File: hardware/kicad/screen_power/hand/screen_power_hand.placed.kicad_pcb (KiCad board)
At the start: 4 copper layers, 130 x 120 mm, 56 parts, among them J1 AUX 5V INPUT, J101 PI USB, J102 TOUCH, J103 EVM 5V, J104 EVM CONTROL, J2 SCREEN CONTROL, J201 PI USB, J202 TOUCH, J203 EVM 5V, J204 EVM CONTROL, K101 G6K-2P-RF DC5, K102 G5LE-1 DC5, K201 G6K-2P-RF DC5, K202 G5LE-1 DC5, Q1 2N3904, Q101 2N7000, Q102 2N3906, Q103 IRLZ44NPBF, Q104 2N7000, Q201 2N7000, Q202 2N3906, Q203 IRLZ44NPBF, Q204 2N7000

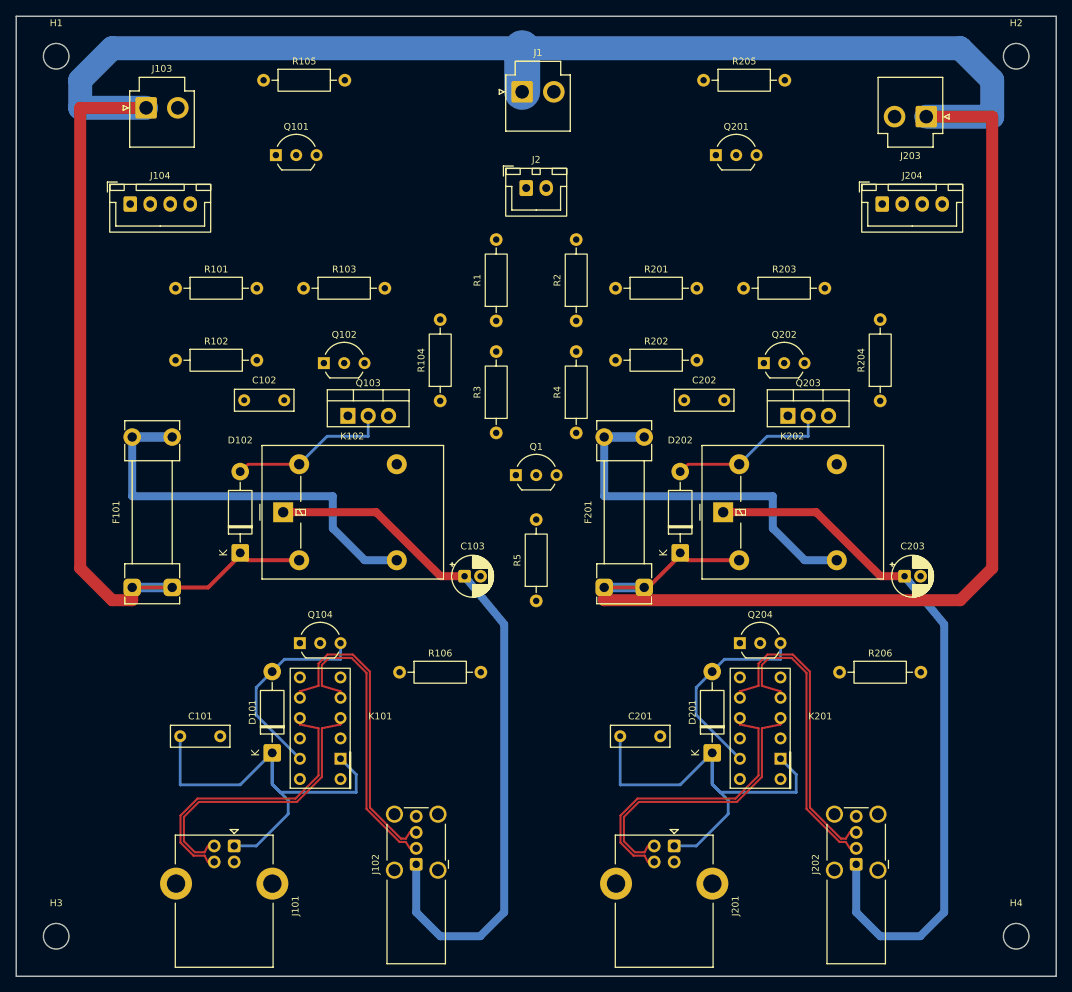
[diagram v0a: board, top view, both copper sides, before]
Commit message: refactor(hardware): simplify and compact screen power boards
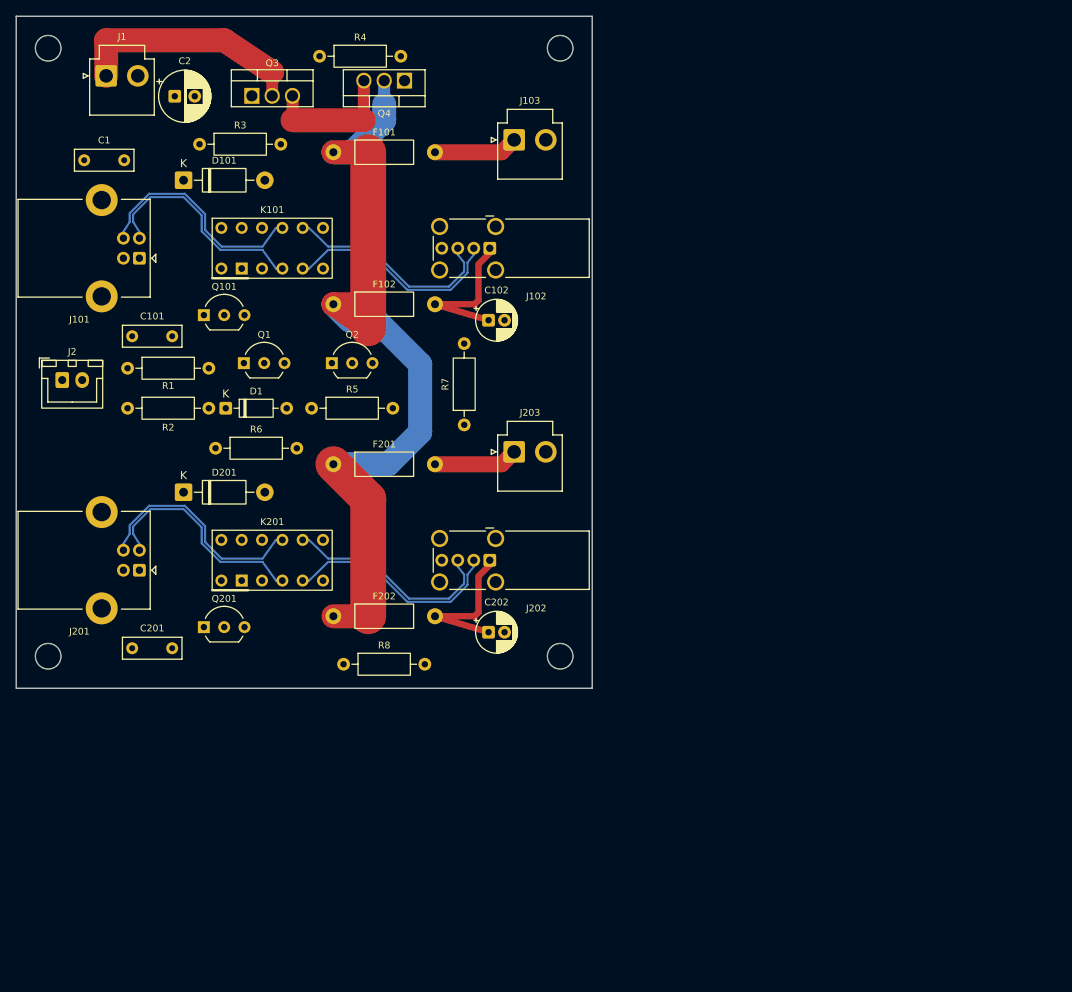
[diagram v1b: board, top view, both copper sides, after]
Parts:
- removed C103, C203: 150uF 10V, CP_Radial_D5.0mm_P2.00mm
- removed D102, D202: 1N4007, D_DO-41_SOD81_P10.16mm_Horizontal
- removed J104, J204: EVM CONTROL, JST_XH_B4B-XH-A_1x04_P2.50mm_Vertical
- removed K102, K202: G5LE-1 DC5, Relay_SPDT_Omron-G5LE-1
- removed Q102, Q202: 2N3906, TO-92_Inline_Wide
- removed Q103, Q203: IRLZ44NPBF, TO-220-3_Vertical
- removed Q104, Q204: 2N7000, TO-92_Inline_Wide
- removed R101, R103, R104, R201, R203, R204: 100k 1%, R_Axial_DIN0207_L6.3mm_D2.5mm_P10.16mm_Horizontal
- removed R102, R202: 5.6k 1%, R_Axial_DIN0207_L6.3mm_D2.5mm_P10.16mm_Horizontal
- removed R105, R106, R205, R206: 100R 1W 1%, R_Axial_DIN0207_L6.3mm_D2.5mm_P10.16mm_Horizontal
- added C1: 100nF 63V, C_Rect_L7.2mm_W2.5mm_P5.00mm, F.Cu at (8.50, 18.0)
- added C2: 220uF 10V, CP_Radial_D6.3mm_P2.50mm, F.Cu at (19.8, 10.0)
- added D1: 1N4148, D_DO-35_SOD27_P7.62mm_Horizontal, F.Cu at (26.2, 49.0)
- added F102: 750mA fast, Fuse_Littelfuse_251_P12.70mm, F.Cu at (39.6, 36.0)
- added F202: 750mA fast, Fuse_Littelfuse_251_P12.70mm, F.Cu at (39.6, 75.0)
- added Q2: 2N3906, TO-92_Inline_Wide, F.Cu at (39.5, 43.4)
- added Q3: SUP70101EL, TO-220-3_SUP70101EL, F.Cu at (29.5, 9.95)
- added Q4: SUP70101EL, TO-220-3_SUP70101EL, F.Cu at (48.5, 8.05)
- added R6: 100k 1%, R_Axial_DIN0207_L6.3mm_D2.5mm_P10.16mm_Horizontal, F.Cu at (24.9, 54.0)
- added R7: 100k 1%, R_Axial_DIN0207_L6.3mm_D2.5mm_P10.16mm_Horizontal, F.Cu at (56.0, 51.1)
- added R8: 100R 1W 1%, R_Axial_DIN0207_L6.3mm_D2.5mm_P10.16mm_Horizontal, F.Cu at (40.9, 81.0)
- C102, C202: value 100nF 63V -> 150uF 10V; footprint C_Rect_L7.2mm_W2.5mm_P5.00mm -> CP_Radial_D5.0mm_P2.00mm
- F101, F201: value 0.8A fast / two clips -> 4A fast; footprint Fuseholder_Clip-5x20mm_Littelfuse_111_Lateral_P18.80x5.00mm_D1.17mm_Horizontal -> Fuse_Littelfuse_251_P12.70mm
- J103: value EVM 5V -> SCREEN 1 POWER
- J2: value SCREEN CONTROL -> GPIO17 / GND
- J203: value EVM 5V -> SCREEN 2 POWER
- R2: value 10k 1% -> 100k 1%
- R3: value 10k 1% -> 4.7k 1%
- R4: value 100k 1% -> 330k 1%
- R5: value 10k 1% -> 5.6k 1%
- moved Q201 87.0 mm to (23.5, 76.4)
- moved J102 77.6 mm to (59.2, 29.0), turned to 180 degrees
- moved J201 75.2 mm to (15.4, 69.2), turned to 180 degrees
- moved J101 74.4 mm to (15.4, 30.2), turned to 180 degrees
- moved D201 73.7 mm to (20.9, 59.5), turned to 0 degrees
- moved D101 72.4 mm to (20.9, 20.5), turned to 0 degrees
- moved H4 66.9 mm to (68.0, 80.0)
- moved J203 66.4 mm to (62.2, 54.5), turned to 0 degrees
- moved K201 64.5 mm to (32.0, 68.0), turned to 0 degrees
- moved J2 62.8 mm to (5.75, 45.5)
- moved C201 62.0 mm to (14.5, 79.0)
- moved K101 60.3 mm to (32.0, 29.0), turned to 0 degrees
- moved F101 59.9 mm to (39.6, 17.0), turned to 0 degrees
- moved J202 59.5 mm to (59.2, 68.0), turned to 180 degrees
- moved R2 57.1 mm to (13.9, 49.0), turned to 0 degrees
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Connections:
- C102 pad 1: AUX_5V -> S1_TOUCH_5V
- C202 pad 1: AUX_5V -> S2_TOUCH_5V
- F101 pad 1: AUX_5V -> SWITCHED_5V
- F101 pad 2: S1_TOUCH_FUSED -> S1_MAIN_5V
- F201 pad 1: AUX_5V -> SWITCHED_5V
- F201 pad 2: S2_TOUCH_FUSED -> S2_MAIN_5V
- J103 pad 1: AUX_5V -> S1_MAIN_5V
- J203 pad 1: AUX_5V -> S2_MAIN_5V
- Q1 pad 2: DUMP_BASE -> CONTROL_BASE
- Q1 pad 3: DISCHARGE -> CONTROL_SINK
- Q101 pad 2: DISCHARGE -> DATA_ENABLE
- Q101 pad 3: S1_MAIN_DUMP -> S1_DATA_COIL_LOW
- Q201 pad 2: DISCHARGE -> DATA_ENABLE
- Q201 pad 3: S2_MAIN_DUMP -> S2_DATA_COIL_LOW
- R1 pad 2: DISPLAY_ENABLE -> CONTROL_BASE
- R2 pad 1: DISPLAY_ENABLE -> CONTROL_BASE
- R3 pad 1: DISPLAY_ENABLE -> CONTROL_SINK
- R3 pad 2: DUMP_BASE -> POWER_GATE
- R4 pad 1: DUMP_BASE -> POWER_GATE
- R4 pad 2: GND -> COMMON_SOURCE
- R5 pad 1: AUX_5V -> BUFFER_SINK
- R5 pad 2: DISCHARGE -> BUFFER_BASE
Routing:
- net AUX_5V: track 391.7 -> 29.4 mm
- net SWITCHED_5V: track 0.00 -> 109.1 mm
- net S2_TOUCH_5V: track 89.2 -> 19.7 mm
- net S1_TOUCH_5V: track 89.2 -> 19.7 mm
- net HOST1_5V: track 55.9 -> 0.00 mm
- net HOST2_5V: track 55.9 -> 0.00 mm
- net S1_TOUCH_FUSED: track 51.1 -> 0.00 mm
- net S2_TOUCH_FUSED: track 47.1 -> 0.00 mm
- net S2_DATA_COIL_LOW: track 25.2 -> 0.00 mm
- net S1_DATA_COIL_LOW: track 25.2 -> 0.00 mm
- net S2_POWER_COIL_LOW: track 20.4 -> 0.00 mm
- net S1_POWER_COIL_LOW: track 20.4 -> 0.00 mm
- net COMMON_SOURCE: track 0.00 -> 16.9 mm
- net S1_DN_P: track 38.6 -> 27.2 mm
- net S2_DN_P: track 38.6 -> 27.2 mm
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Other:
- board size 130 x 120 mm -> 72 x 84 mm

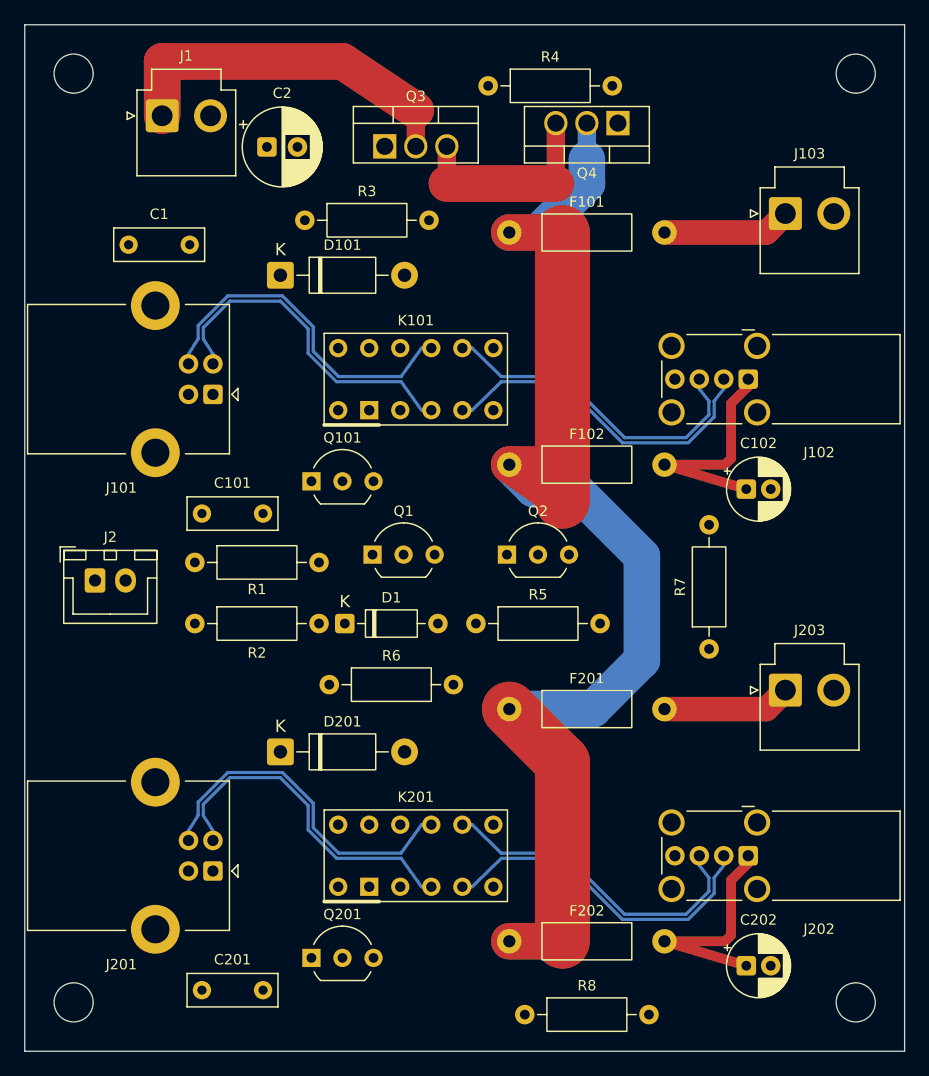
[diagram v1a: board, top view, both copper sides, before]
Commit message: feat(hardware): publish screen switching and board refinements
Add the hand-soldered two-layer screen-power board, aligned console connectors, ADC supply isolation, white ring carrier and reviewed manufacturing ZIPs. Integrate GPIO17 ownership with Weston startup and shutdown; retain assembled-system validation as the hardware gate.
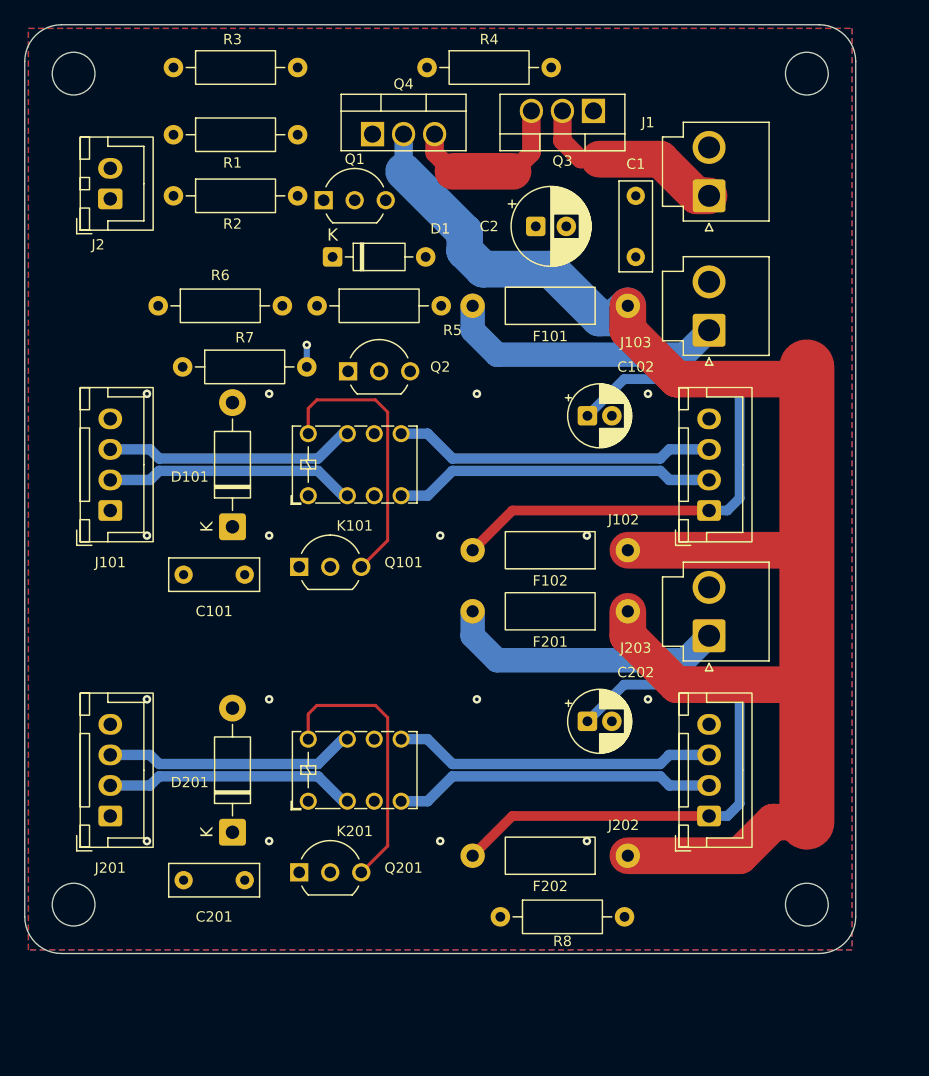
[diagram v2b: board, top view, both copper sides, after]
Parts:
- H1, H2, H3, H4: footprint MountingHole_3.2mm_M3 -> MountingHole_3.5mm
- J101, J201: value PI USB -> PI USB / XH4; footprint USB_B_Lumberg_2411_06_Horizontal -> JST_XH_B4B-XH-A_1x04_P2.50mm_Vertical
- J102, J202: value TOUCH -> TOUCH / XH4; footprint USB_A_Wuerth_614004134726_Horizontal -> JST_XH_B4B-XH-A_1x04_P2.50mm_Vertical
- K101, K201: value G6K-2P-RF DC5 -> IM03TS; footprint Relay_DPDT_Omron_G6K-2P-RF -> Relay_DPDT_AXICOM_IMSeries_Pitch5.08mm_D0.90mm
- moved R7 48.9 mm to (12.9, 28.0), turned to 0 degrees
- moved J1 45.2 mm to (56.0, 14.0), turned to 90 degrees
- moved C1 41.5 mm to (50.0, 19.0), turned to 90 degrees
- moved R1 35.0 mm to (12.2, 9.00)
- moved R2 35.0 mm to (12.2, 14.0)
- moved R6 34.0 mm to (10.9, 23.0)
- moved J2 31.3 mm to (7.00, 14.2), turned to 90 degrees
- moved D1 30.0 mm to (25.2, 19.0)
- moved Q1 29.3 mm to (24.5, 14.4)
- moved R5 29.1 mm to (23.9, 23.0)
- moved C202 23.9 mm to (46.0, 57.0)
- moved C2 22.9 mm to (41.8, 16.5)
- moved D101 21.0 mm to (17.0, 41.1), turned to 90 degrees
- moved Q4 20.1 mm to (28.5, 8.95), turned to 0 degrees
- moved Q2 19.8 mm to (26.5, 28.4)
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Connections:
- K101 pad 2: (no net) -> S1_UP_N
- K101 pad 3: S1_UP_N -> (no net)
- K101 pad 6: S1_UP_P -> (no net)
- K101 pad 7: (no net) -> S1_UP_P
- K201 pad 2: (no net) -> S2_UP_N
- K201 pad 3: S2_UP_N -> (no net)
- K201 pad 6: S2_UP_P -> (no net)
- K201 pad 7: (no net) -> S2_UP_P
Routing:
- net S2_TOUCH_5V: track 19.7 -> 46.5 mm
- net S1_TOUCH_5V: track 19.7 -> 46.5 mm
- net SWITCHED_5V: track 109.1 -> 132.0 mm
- net S1_DATA_COIL_LOW: track 0.00 -> 22.8 mm
- net S2_DATA_COIL_LOW: track 0.00 -> 22.8 mm
- net AUX_5V: track 29.4 -> 16.3 mm
- net S2_MAIN_5V: track 10.5 -> 23.0 mm
- net S1_MAIN_5V: track 10.5 -> 23.0 mm
- net S1_UP_P: track 28.6 -> 20.6 mm
- net S2_UP_P: track 28.6 -> 20.6 mm
- net S2_UP_N: track 27.9 -> 20.6 mm
- net S1_UP_N: track 27.9 -> 20.6 mm
- net COMMON_SOURCE: track 16.9 -> 14.2 mm
- net GND: track 0.00 -> 1.80 mm, vias 0 -> 17
- net S2_DN_N: track 27.9 -> 26.4 mm
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- added copper zone on B.Cu, net GND
- added copper zone on F.Cu, net GND
- removed copper zone on In1.Cu, net GND
- removed copper zone on In2.Cu, net GND
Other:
- board size 72 x 84 mm -> 68 x 76 mm
- copper layers 4 -> 2

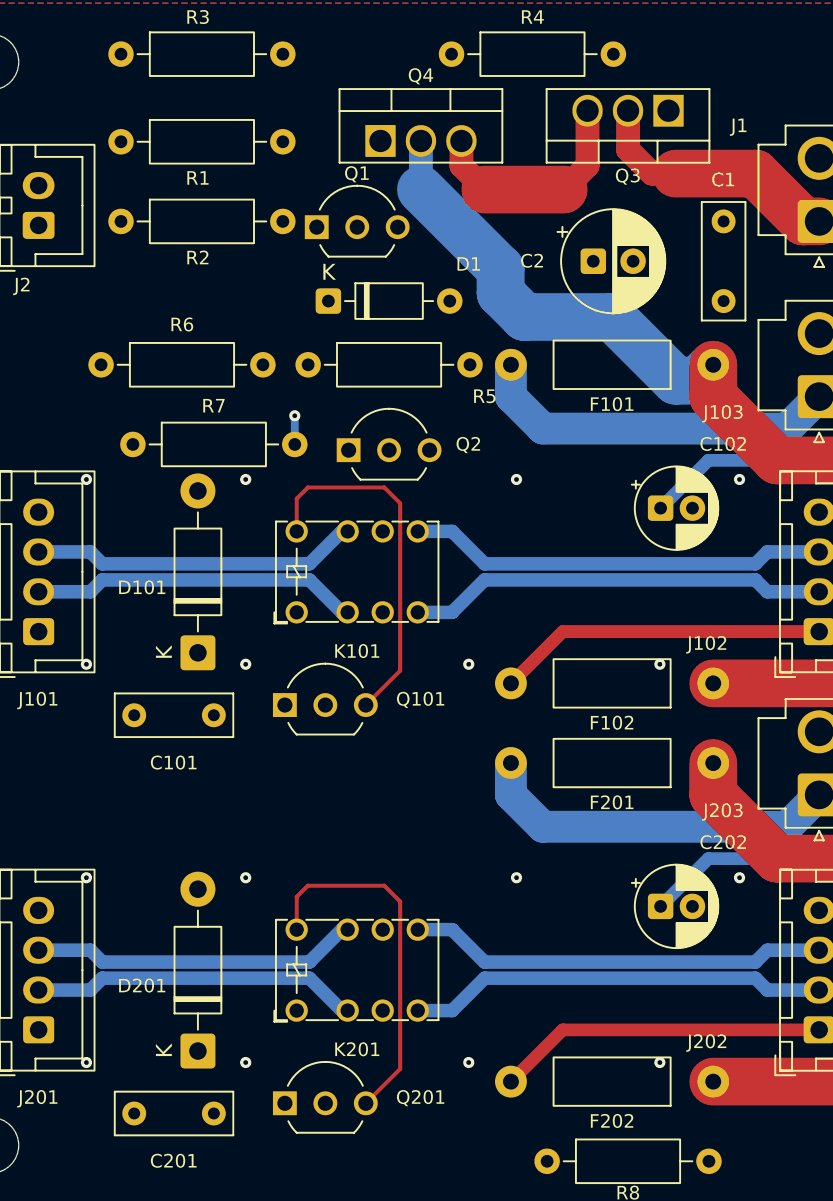
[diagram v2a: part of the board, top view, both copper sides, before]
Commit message: fix(hardware): correct screen relay contacts and strengthen power routing
Replace withdrawn Revision I with checked Revision J fabrication files. Correct USB relay commons, reinforce the shared power paths, and verify relay states and a fuse-barrel-independent via path. Record the requested Claude review and independent follow-up checks.
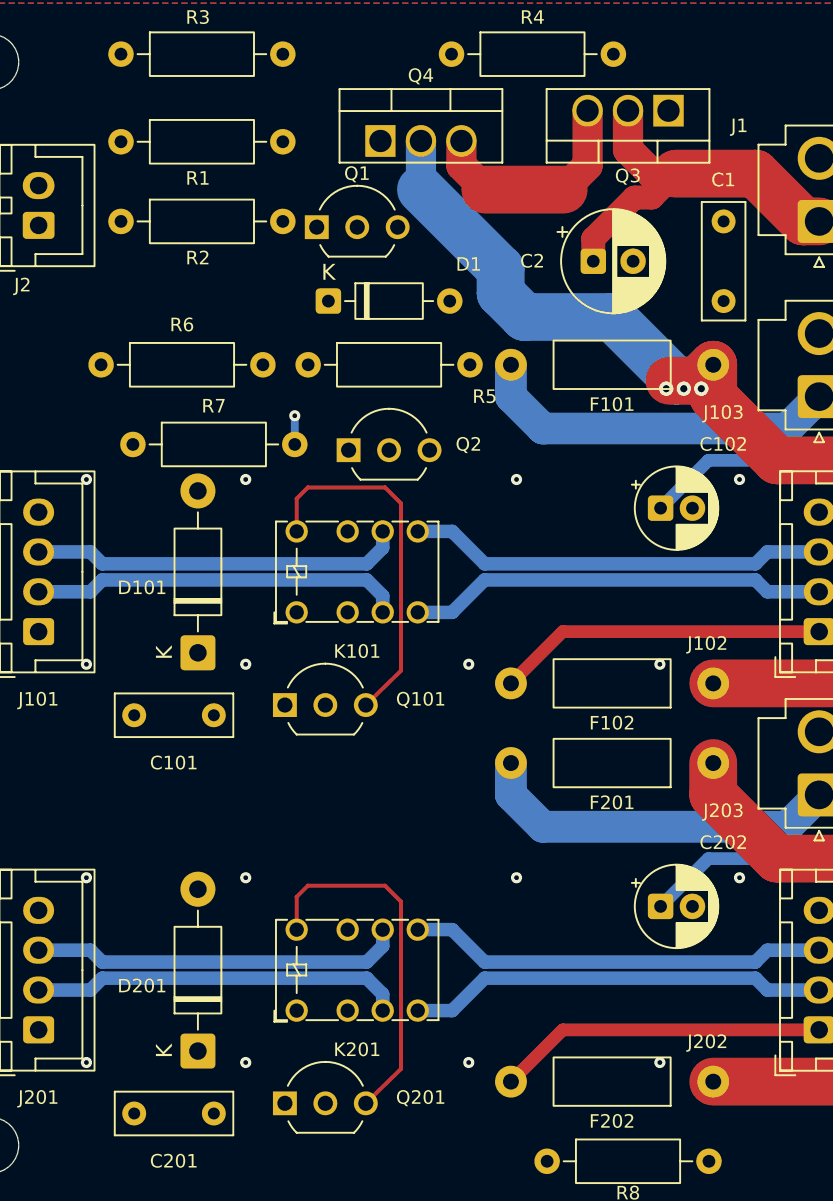
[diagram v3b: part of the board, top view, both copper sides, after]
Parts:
- K101, K201: value IM03TS -> IM02TS
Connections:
- K101 pad 2: S1_UP_N -> (no net)
- K101 pad 3: (no net) -> S1_UP_N
- K101 pad 6: (no net) -> S1_UP_P
- K101 pad 7: S1_UP_P -> (no net)
- K201 pad 2: S2_UP_N -> (no net)
- K201 pad 3: (no net) -> S2_UP_N
- K201 pad 6: (no net) -> S2_UP_P
- K201 pad 7: S2_UP_P -> (no net)
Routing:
- net AUX_5V: track 16.3 -> 24.6 mm
- net SWITCHED_5V: track 132.0 -> 135.1 mm, vias 0 -> 3
- net S1_UP_P: track 20.6 -> 23.4 mm
- net S2_UP_N: track 20.6 -> 23.4 mm
- net S1_UP_N: track 20.6 -> 23.4 mm
- net S2_UP_P: track 20.6 -> 23.4 mm
